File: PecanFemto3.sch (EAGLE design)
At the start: 29 parts

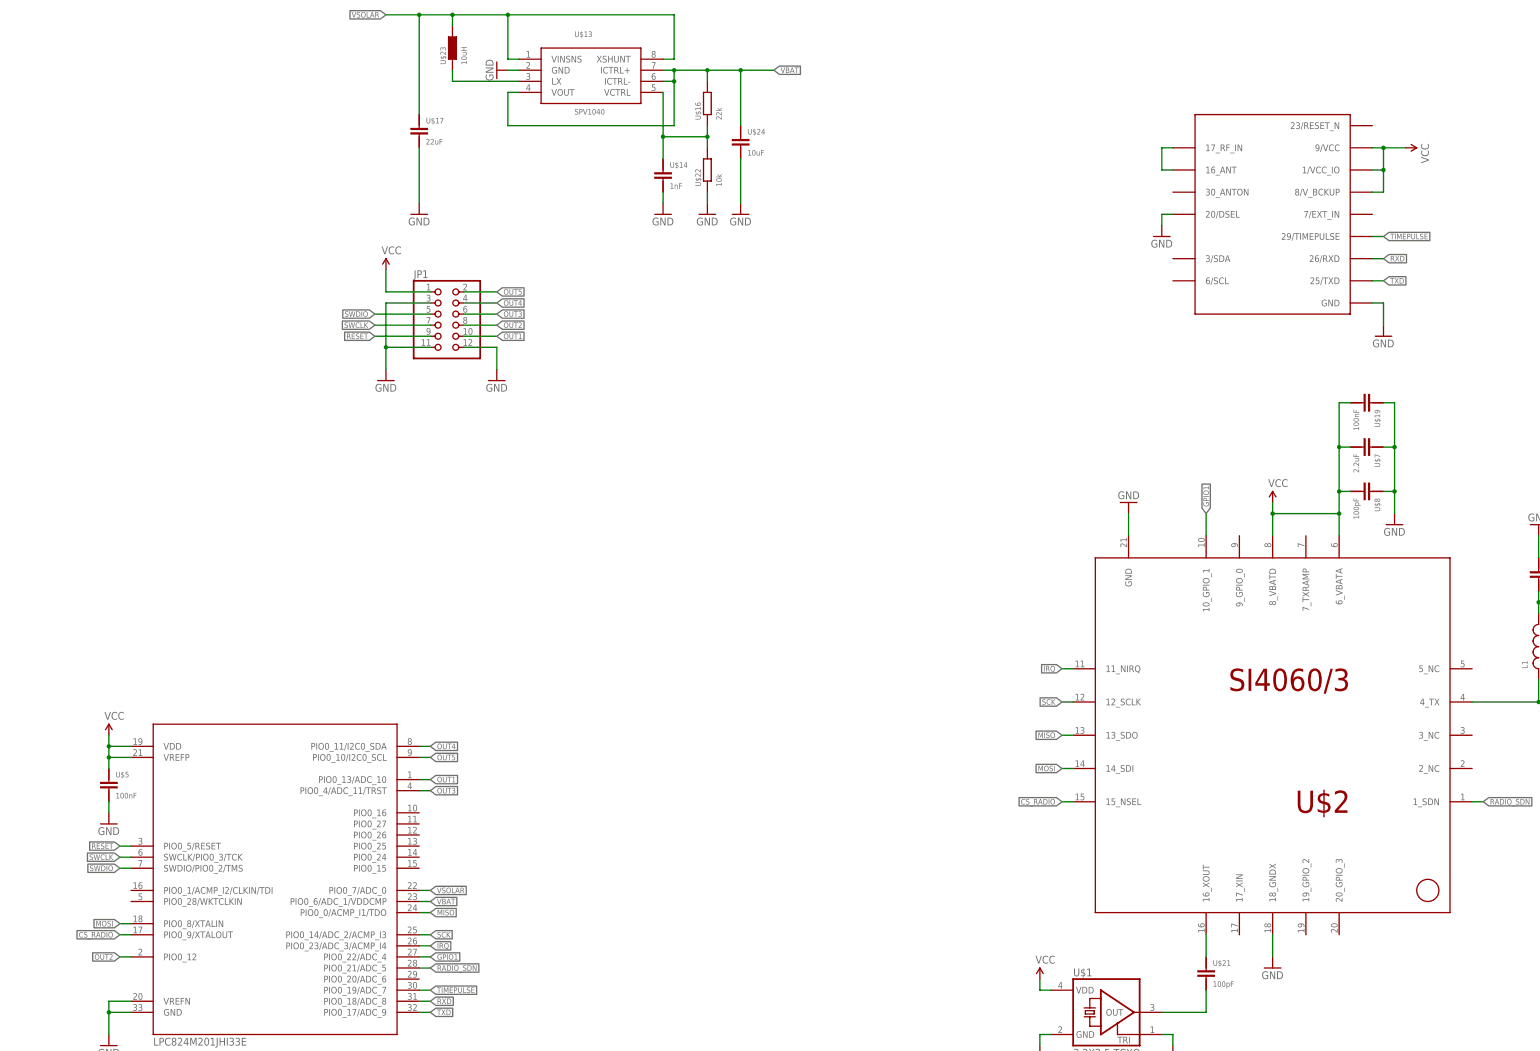
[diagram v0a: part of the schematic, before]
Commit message: Added step down converter
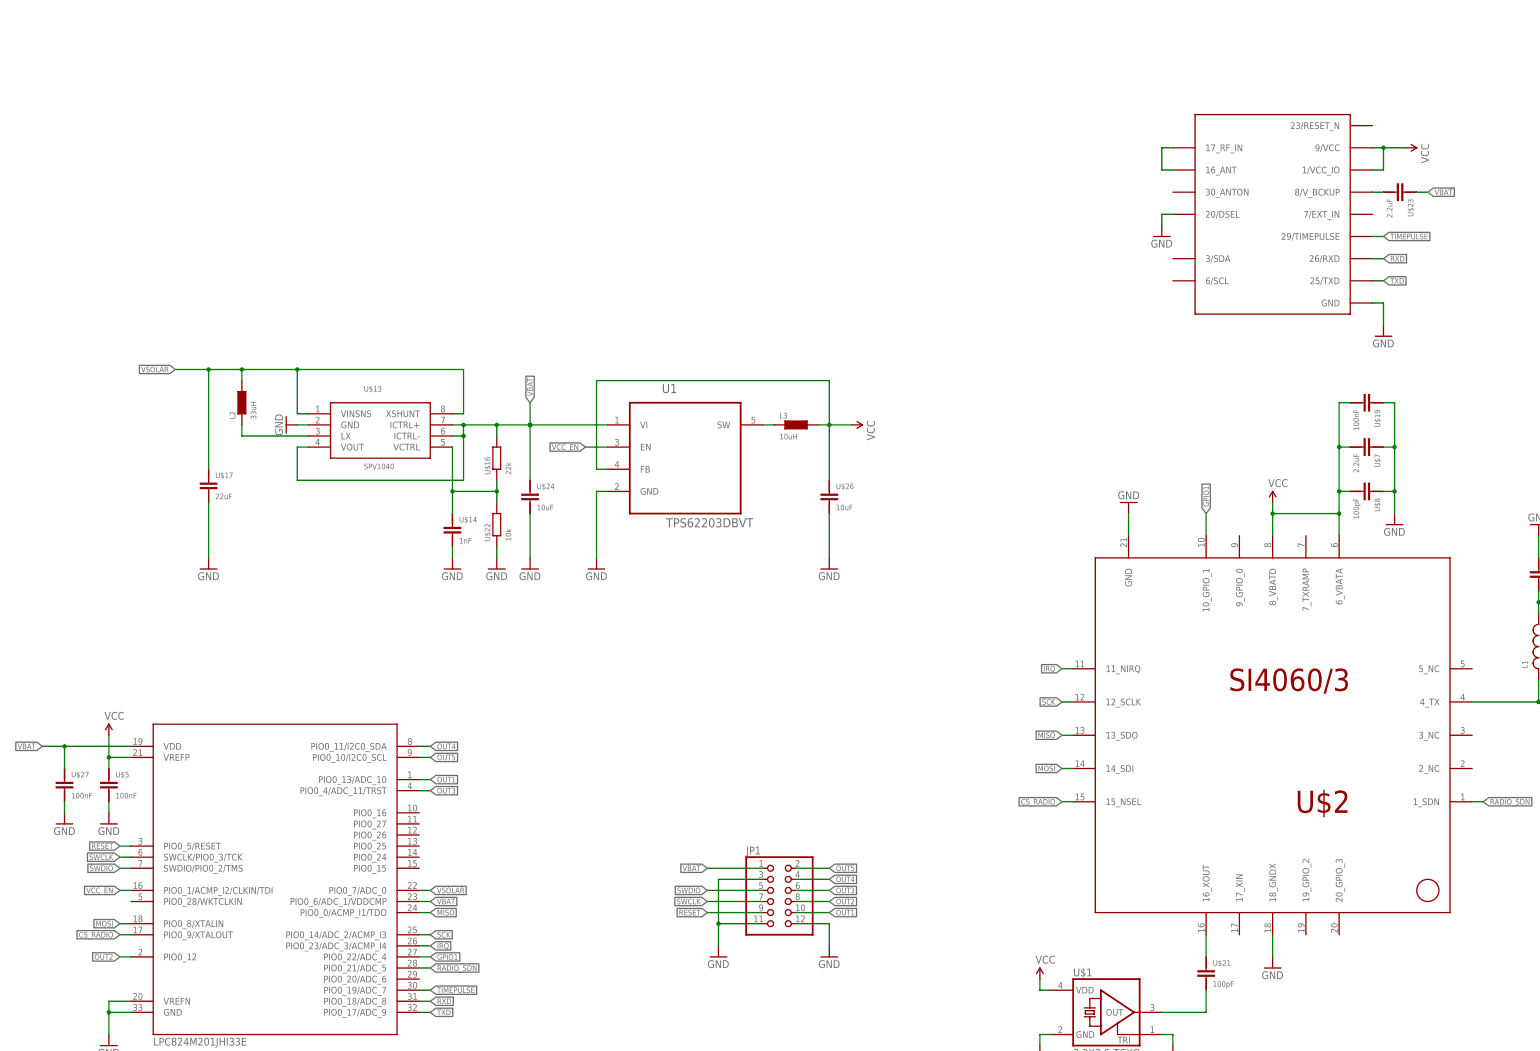
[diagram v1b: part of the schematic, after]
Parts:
- added L2: 33uH, PecanPico6:IND-LPS3015
- added L3: 10uH, PecanPico6:IND-LPS3015
- added U$26: 10uF, sven:CAP-0805
- added U$27: 100nF, sven:CAP-0402
- added U1: TPS62203DBVT, TPS62203:TPS62203DBVT
- U$23: value 10uH -> 2.2uF; device PecanPico6:IND-LPS3015 -> sven:CAP-0603
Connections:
- new net N$1: U$23.1, U$3.8/V_BCKUP
- new net N$15: L3.1, U1.SW
- new net VCC_EN: U$4.PIO0_1/ACMP_I2/CLKIN/TDI, U1.EN
- net GND: now also U$26.1, U$27.1, U1.GND
- net N$14: now also L2.1; no longer U$23.1
- net VBAT: now also JP1.1, U$23.2, U$27.2, U$4.VDD, U1.VI
- net VCC: now also L3.2, U$26.2, U1.FB; no longer JP1.1, U$3.8/V_BCKUP, U$4.VDD
- net VSOLAR: now also L2.2; no longer U$23.2
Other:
- moved on the sheet: JP1, U$13, U$14, U$16, U$17, U$22, U$24

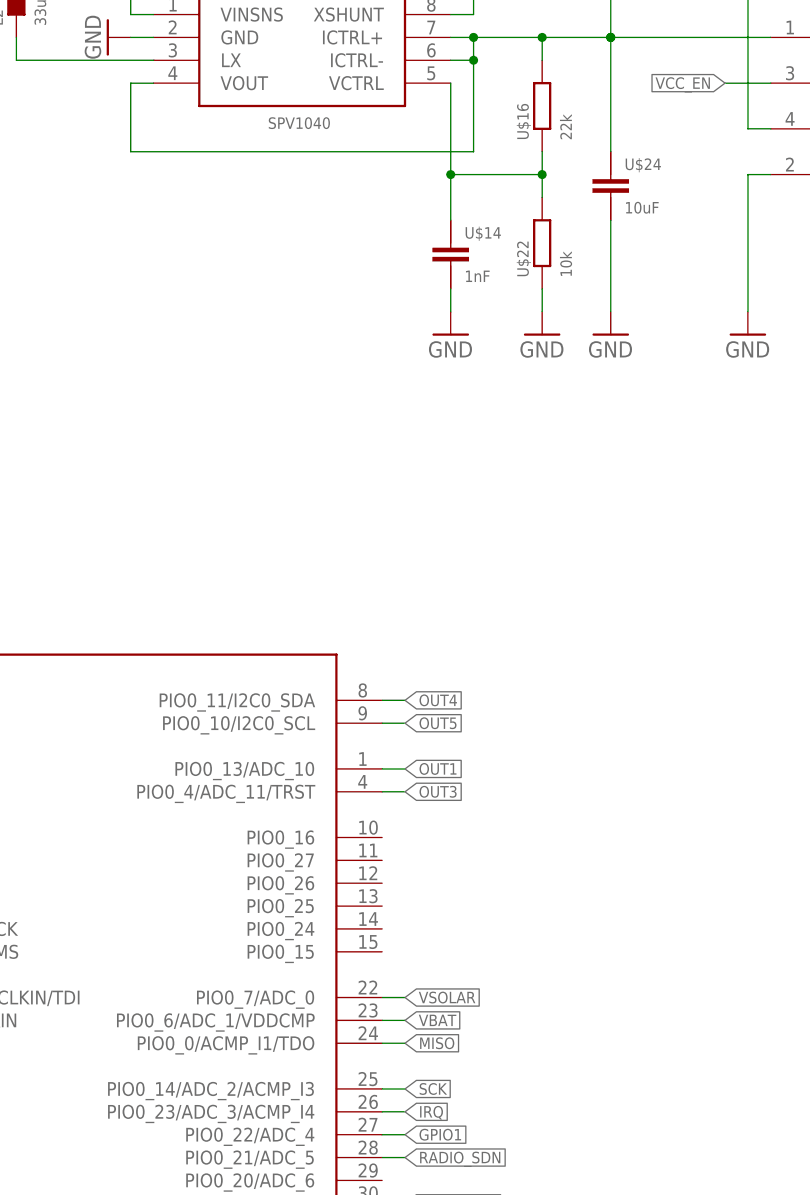
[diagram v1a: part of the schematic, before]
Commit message: Moved components around
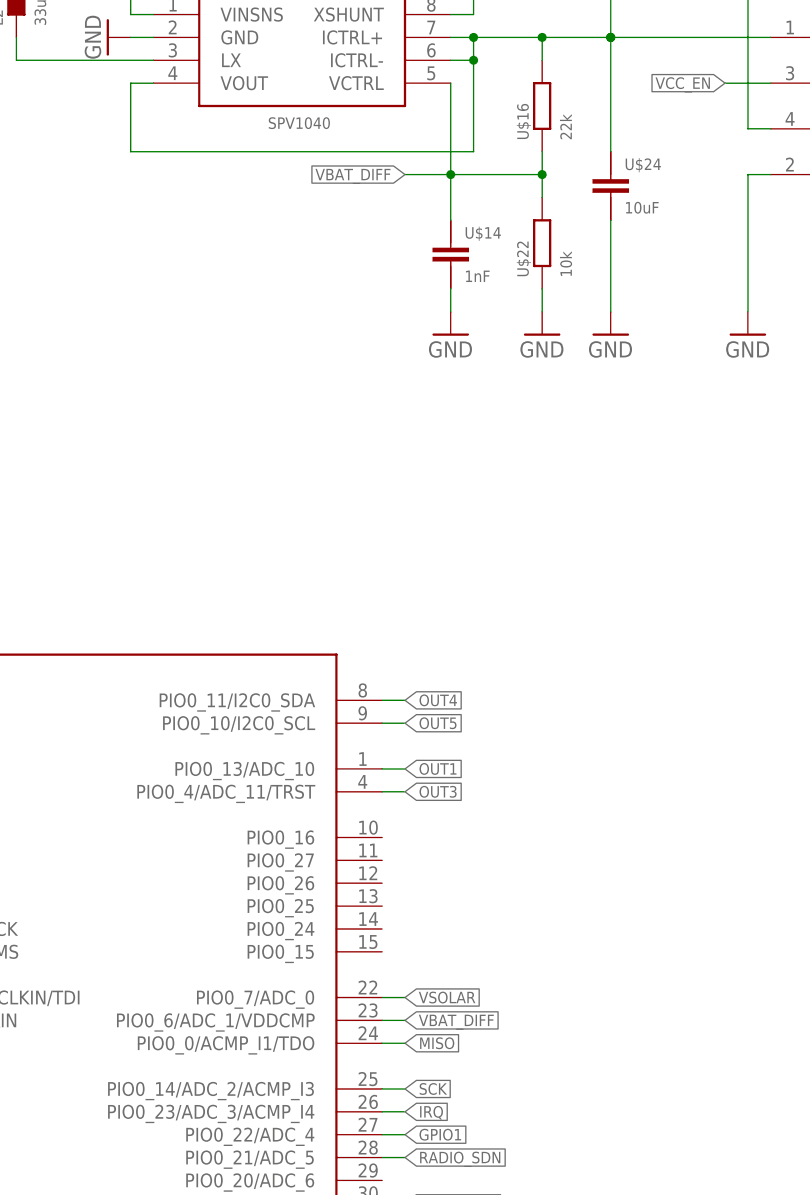
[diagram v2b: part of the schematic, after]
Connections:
- removed net N$17: U$13.VCTRL, U$14.2, U$16.1, U$22.2
- new net VBAT_DIFF: U$13.VCTRL, U$14.2, U$16.1, U$22.2, U$4.PIO0_6/ADC_1/VDDCMP
- net VBAT: no longer U$4.PIO0_6/ADC_1/VDDCMP
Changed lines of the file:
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@@
-</segment>
-<segment>
-<wire x1="22.86" y1="2.54" x2="25.4" y2="2.54" width="0.1524" layer="91"/>
-<label x="25.4" y="2.54" size="1.27" layer="95" xref="yes"/>
-<pinref part="U$4" gate="G$1" pin="PIO0_6/ADC_1/VDDCMP"/>
 </segment>
 <segment>
@@
 </segment>
 </net>
-<net name="N$17" class="0">
+<net name="VBAT_DIFF" class="0">
 <segment>
 <pinref part="U$22" gate="G$1" pin="2"/>
@@
 <junction x="40.64" y="96.52"/>
 <junction x="30.48" y="96.52"/>
+<wire x1="30.48" y1="96.52" x2="25.4" y2="96.52" width="0.1524" layer="91"/>
+<label x="25.4" y="96.52" size="1.27" layer="95" rot="R180" xref="yes"/>
+</segment>
+<segment>
+<wire x1="22.86" y1="2.54" x2="25.4" y2="2.54" width="0.1524" layer="91"/>
+<label x="25.4" y="2.54" size="1.27" layer="95" xref="yes"/>
+<pinref part="U$4" gate="G$1" pin="PIO0_6/ADC_1/VDDCMP"/>
 </segment>
 </net>

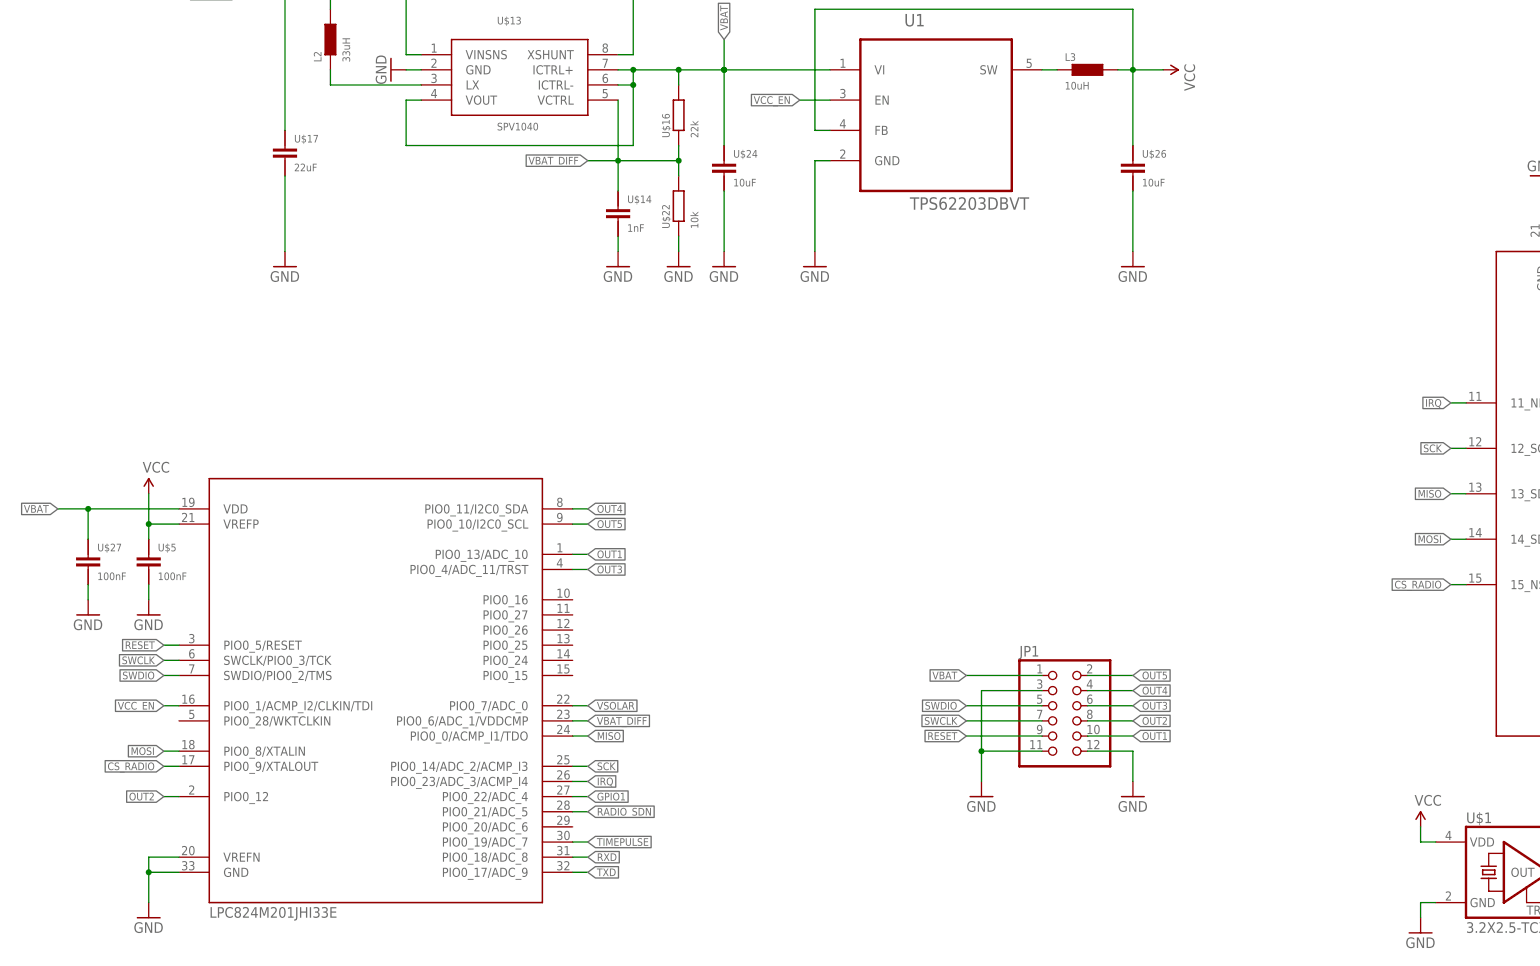
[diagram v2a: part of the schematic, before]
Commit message: Moved parts around
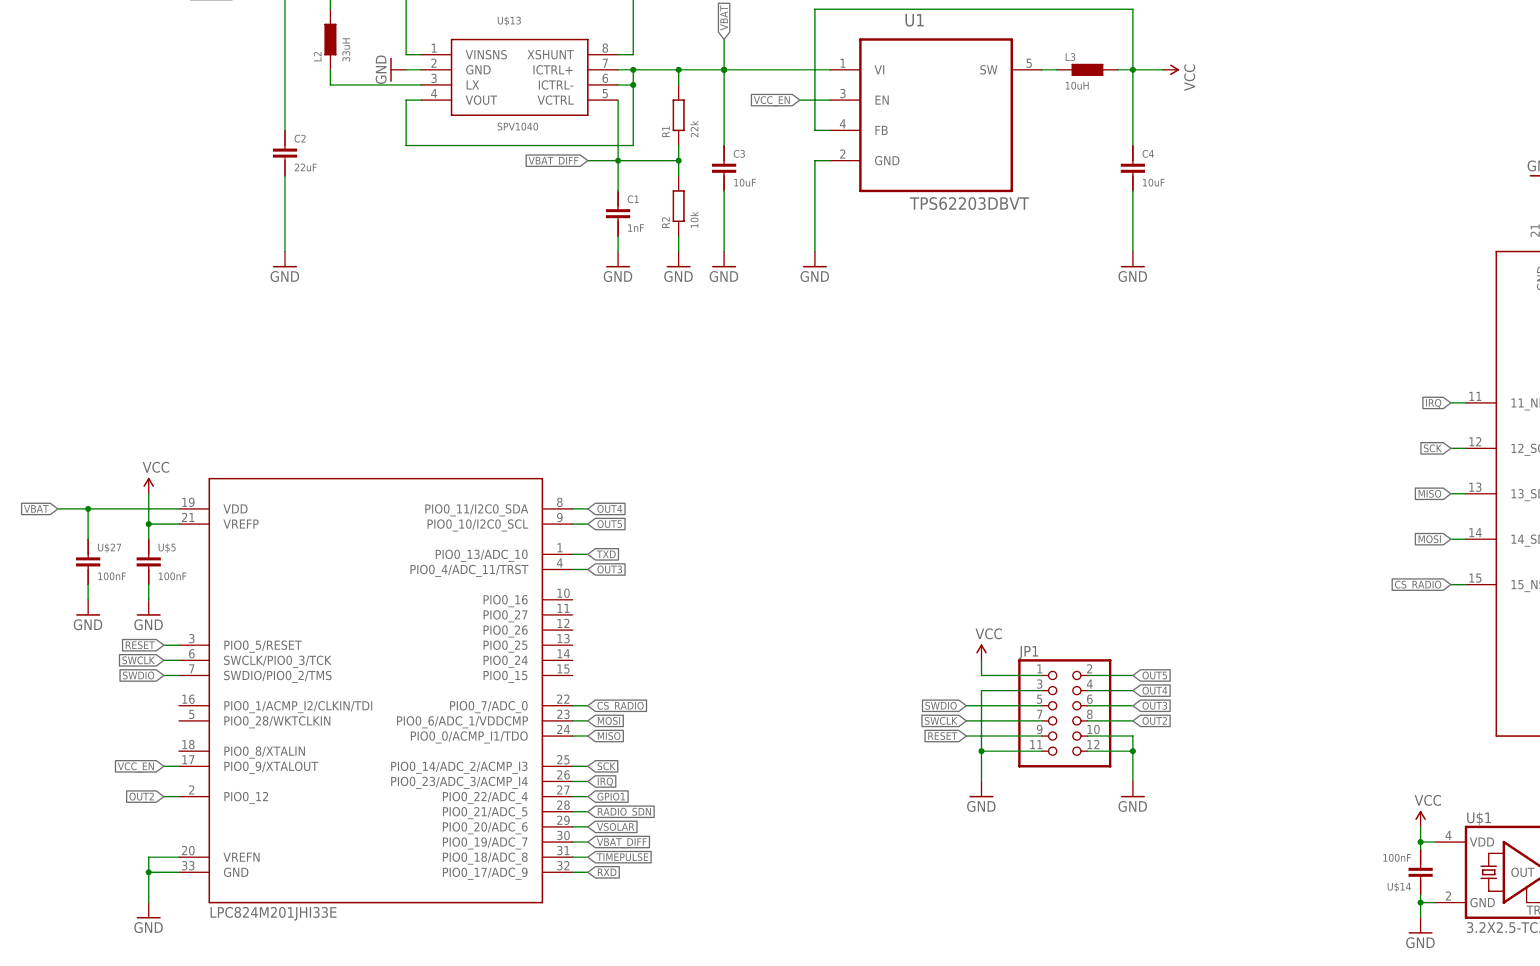
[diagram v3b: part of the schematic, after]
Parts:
- added C1: 1nF, sven:CAP-0402
- U$14: value 1nF -> 100nF
- U$7: device sven:CAP-0603 -> sven:CAP-0402
- renumbered U$16 to R1, U$17 to C2, U$22 to R2, U$24 to C3, U$26 to C4
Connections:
- removed net OUT1: JP1.10, U$4.PIO0_13/ADC_10
- net CS_RADIO: now also U$4.PIO0_7/ADC_0; no longer U$4.PIO0_9/XTALOUT
- net GND: now also C1.1, JP1.10, U$14.2; no longer U$14.1
- net MOSI: now also U$4.PIO0_6/ADC_1/VDDCMP; no longer U$4.PIO0_8/XTALIN
- net RXD: now also U$4.PIO0_17/ADC_9; no longer U$4.PIO0_18/ADC_8
- net TIMEPULSE: now also U$4.PIO0_18/ADC_8; no longer U$4.PIO0_19/ADC_7
- net TXD: now also U$4.PIO0_13/ADC_10; no longer U$4.PIO0_17/ADC_9
- net VBAT: no longer JP1.1
- net VBAT_DIFF: now also C1.2, U$4.PIO0_19/ADC_7; no longer U$14.2, U$4.PIO0_6/ADC_1/VDDCMP
- net VCC: now also JP1.1, U$14.1
- net VCC_EN: now also U$4.PIO0_9/XTALOUT; no longer U$4.PIO0_1/ACMP_I2/CLKIN/TDI
- net VSOLAR: now also U$4.PIO0_20/ADC_6; no longer U$4.PIO0_7/ADC_0
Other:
- moved on the sheet: U$14
